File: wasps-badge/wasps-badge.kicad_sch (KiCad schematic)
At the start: 23 parts, among them J1 Conn_Debug, J2 Conn_AddOn, J3 Conn_CTF, SW1 SW_SPDT, SW2 SW_Push, SW3 SW_Push, U1 CH32V003FxPx

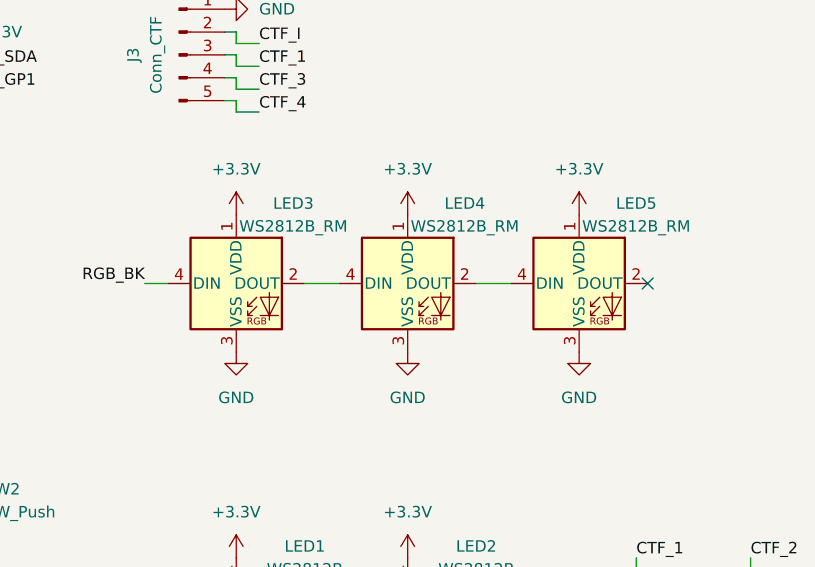
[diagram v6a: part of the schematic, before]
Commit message: Remove reverse-mount LEDs from BOM and placement
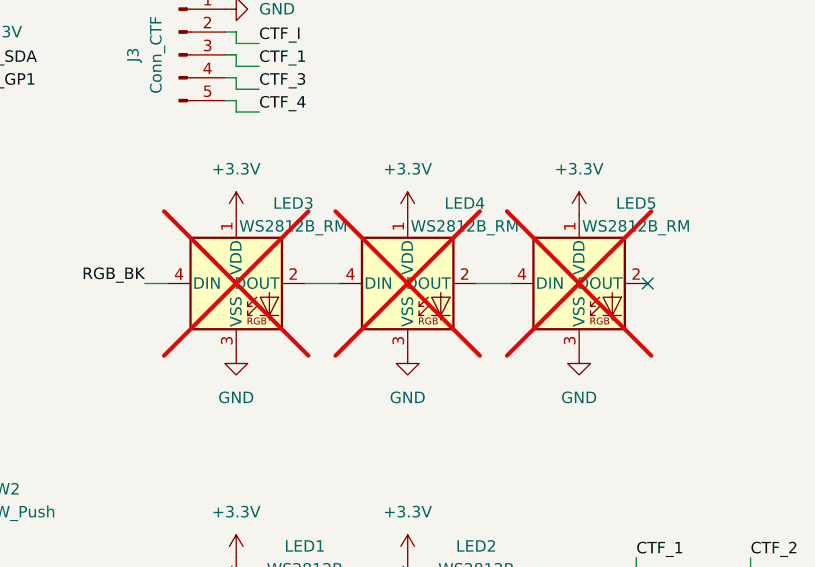
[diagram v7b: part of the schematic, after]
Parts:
- LED3, LED4, LED5: now not fitted; now left out of the parts list
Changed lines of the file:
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@@
 		(unit 1)
 		(exclude_from_sim no)
-		(in_bom yes)
-		(on_board yes)
-		(dnp no)
+		(in_bom no)
+		(on_board yes)
+		(dnp yes)
 		(property "Reference" "LED4"
 			(at 184.15 54.61 0)
@@
 		(unit 1)
 		(exclude_from_sim no)
-		(in_bom yes)
-		(on_board yes)
-		(dnp no)
+		(in_bom no)
+		(on_board yes)
+		(dnp yes)
 		(property "Reference" "LED3"
 			(at 165.1 54.61 0)
@@
 		(unit 1)
 		(exclude_from_sim no)
-		(in_bom yes)
-		(on_board yes)
-		(dnp no)
+		(in_bom no)
+		(on_board yes)
+		(dnp yes)
 		(property "Reference" "LED5"
 			(at 203.2 54.61 0)
